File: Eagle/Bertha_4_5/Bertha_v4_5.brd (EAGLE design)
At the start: 100 x 84.6 mm, 136 parts, among them CON1 JACK_DC_BARREL, CON2 JACK_DC_BARREL, IC1 MCP1703DB, IC4 DRV8811, J1 RJ12RIGHTANGLE-I2C, J2 RJ12RIGHTANGLE-I2C, Q5 BSP75, Q6 BSP75, U1 HX711, U100 RN2483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

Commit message: All connectors on the connector slot
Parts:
- removed JP1: (no value), freetronics-master-v1:SCREWTERMINAL-3.5MM-4
- added JP3: (no value), jumper:JP4
- moved X1 37.1 mm to (7.61, -2.08), turned to 180 degrees
- moved CON2 33.7 mm to (19.7, -5.27), turned to 0 degrees
- moved LDM1 26.7 mm to (75.8, 28.6)
- moved R11 26.2 mm to (27.6, 27.7), turned to 270 degrees
- moved RT1 25.7 mm to (8.58, 4.91), turned to 180 degrees
- moved RK11 25.2 mm to (73.2, 30.7)
- moved LDM4 20.5 mm to (78.1, 23.9)
- moved CU8 18.0 mm to (0.41, 19.3), turned to 270 degrees
- moved LDPID 17.1 mm to (24.8, 32.3), turned to 0 degrees
- moved RK8 15.0 mm to (74.0, 25.3)
- moved LDPW12 14.7 mm to (22.3, 32.3), turned to 0 degrees
- moved HX1 13.8 mm to (8.35, 21.2), turned to 180 degrees
- moved RK14 13.5 mm to (24.9, 27.7), turned to 270 degrees
- moved LDPW3 12.9 mm to (19.8, 32.2), turned to 0 degrees
- moved CU7 12.0 mm to (7.25, 12.9), turned to 180 degrees
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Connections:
- net N$10: now also JP3.2; no longer JP1.3
- net N$4: now also JP3.4; no longer JP1.1
- net N$55: now also JP3.1; no longer JP1.4
- net N$56: now also JP3.3; no longer JP1.2
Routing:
- net VDD: track 183.1 -> 119.0 mm, vias 2 -> 1
- net +12V: track 205.8 -> 158.6 mm
- net D6*: track 61.4 -> 26.9 mm
- net N$21: track 22.0 -> 51.6 mm
- net A1: track 48.1 -> 23.5 mm, vias 2 -> 0
- net N$6: track 21.9 -> 2.69 mm
- net N$9: track 35.1 -> 19.1 mm
- net 3.3V: track 430.3 -> 437.7 mm
- net VUSB: track 116.9 -> 113.2 mm
- net N$31: track 1.82 -> 0.00 mm
- net N$37: track 1.80 -> 0.00 mm
- net N$2: track 15.6 -> 17.4 mm
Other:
- board text added: "12V"

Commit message: All connectors BUT the PID on external slot, DRV8811 to be routed closes #57 ref #47
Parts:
- moved CON2 43.3 mm to (-4.99, 30.3), turned to 270 degrees
- moved R11 14.9 mm to (19.2, 15.3), turned to 180 degrees
- moved LDPID 14.3 mm to (23.9, 18.0), turned to 270 degrees
- moved RT1 13.2 mm to (21.7, 3.35)
- moved X1 13.1 mm to (20.7, -2.00)
- moved LDPW12 11.8 mm to (23.8, 20.5), turned to 270 degrees
- moved RK14 11.3 mm to (19.3, 17.9), turned to 180 degrees
- moved C2 10.6 mm to (39.6, 19.2), turned to 90 degrees
- moved LDPW3 9.98 mm to (23.8, 23.0), turned to 270 degrees
- moved HX1 9.87 mm to (7.40, 11.4), turned to 0 degrees
- moved CU4 9.32 mm to (37.3, 19.2), turned to 90 degrees
- moved U$2 8.31 mm to (20.6, 32.6)
- moved 3V3 8.31 mm to (24.8, 29.1)
- moved RT2 8.31 mm to (23.9, 32.6)
- moved R12 7.75 mm to (19.3, 20.6), turned to 180 degrees
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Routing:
- net 3.3V: track 437.7 -> 486.7 mm, vias 14 -> 16
- net +12V: track 158.6 -> 205.6 mm
- net VDD: track 119.0 -> 159.1 mm, vias 1 -> 2
- net N$21: track 51.6 -> 79.3 mm
- net N$6: track 2.69 -> 26.4 mm
- net D6*: track 26.9 -> 50.0 mm
- net N$9: track 19.1 -> 28.6 mm
- net N$2: track 17.4 -> 19.4 mm
- net GND: track 160.9 -> 162.4 mm

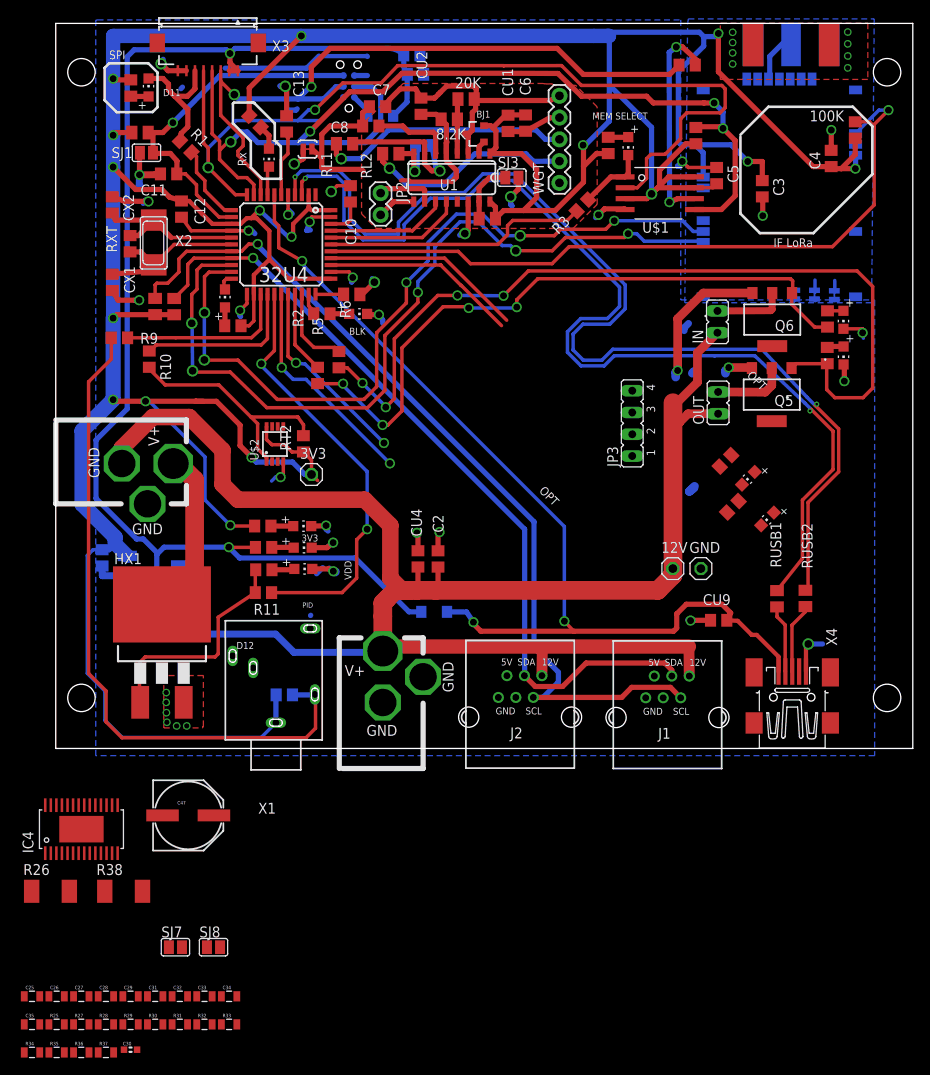
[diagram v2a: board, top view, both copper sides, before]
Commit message: Bertha V4.5 with DRV8811, still need to put the connectors closer to the edge ref #47
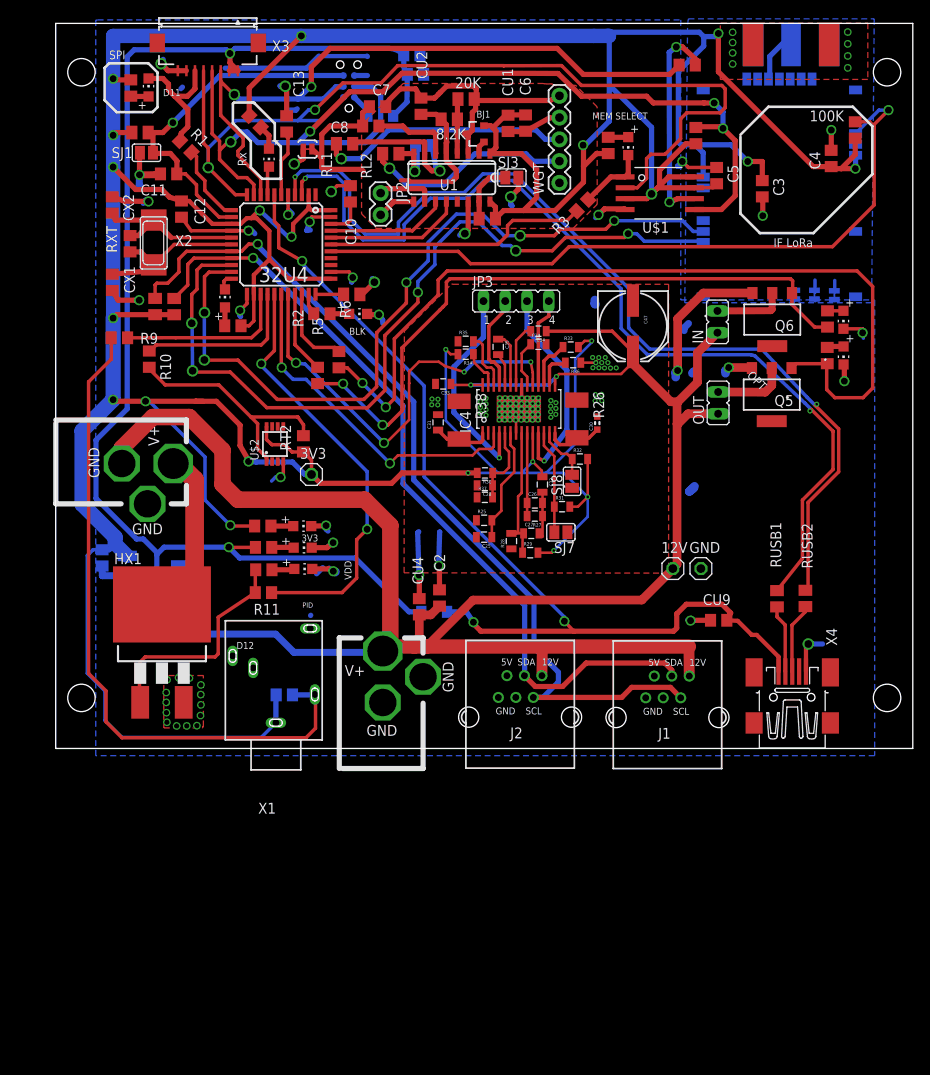
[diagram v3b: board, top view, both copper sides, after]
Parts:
- removed LDM1, LDM4: RED, adafruit:CHIP-LED0805
- removed RK11, RK8: 10K, rcl:R0805
- moved R36 98.8 mm to (55.4, 42.1), turned to 180 degrees
- moved C35 96.0 mm to (46.6, 44.0), turned to 270 degrees
- moved R34 95.9 mm to (42.8, 43.1), turned to 180 degrees
- moved R35 95.7 mm to (42.8, 44.6)
- moved C30 91.2 mm to (58.2, 35.1), turned to 90 degrees
- moved C29 89.7 mm to (51.3, 44.3)
- moved R33 88.5 mm to (55.1, 43.9)
- moved C34 85.6 mm to (51.3, 45.8), turned to 180 degrees
- moved R26 82.5 mm to (55.8, 35.5), turned to 270 degrees
- moved C26 80.2 mm to (50.9, 25.7)
- moved R27 79.5 mm to (50.9, 24.2), turned to 180 degrees
- moved R32 79.2 mm to (56.2, 30.9)
- moved R37 78.4 mm to (45.1, 26.4)
- moved C47 77.1 mm to (62.4, 46.4), turned to 270 degrees
- moved R25 77.1 mm to (45.0, 23.7)
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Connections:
- removed net D3: IC4.3
- removed net D6: IC4.19
- removed net N$31: LDM4.C, RK8.2
- removed net N$37: LDM1.C, RK11.2
- net +12V: no longer LDM1.A, LDM4.A
- net D8*: now also IC4.3
- net D9*: now also IC4.19
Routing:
- net 3.3V: track 486.7 -> 583.7 mm, vias 16 -> 22
- net +12V: track 205.6 -> 244.7 mm, vias 0 -> 2
- net D9*: track 22.5 -> 50.4 mm, vias 2 -> 4
- net N$56: track 0.00 -> 25.1 mm, vias 0 -> 1
- net N$55: track 0.00 -> 24.8 mm, vias 0 -> 1
- net A1: track 23.5 -> 0.00 mm
- net A0: track 22.8 -> 0.00 mm
- net GND: track 162.4 -> 184.3 mm, vias 36 -> 117
- net N$49: track 0.00 -> 15.7 mm
- net D8*: track 25.9 -> 40.4 mm
- net N$45: track 0.00 -> 13.4 mm
- net USB_P: track 124.4 -> 111.2 mm
- net USB_N: track 122.7 -> 109.6 mm
- net N$51: track 0.00 -> 12.1 mm
- net N$10: track 0.00 -> 11.3 mm
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
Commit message: shortened boards by 1mm, closes #68
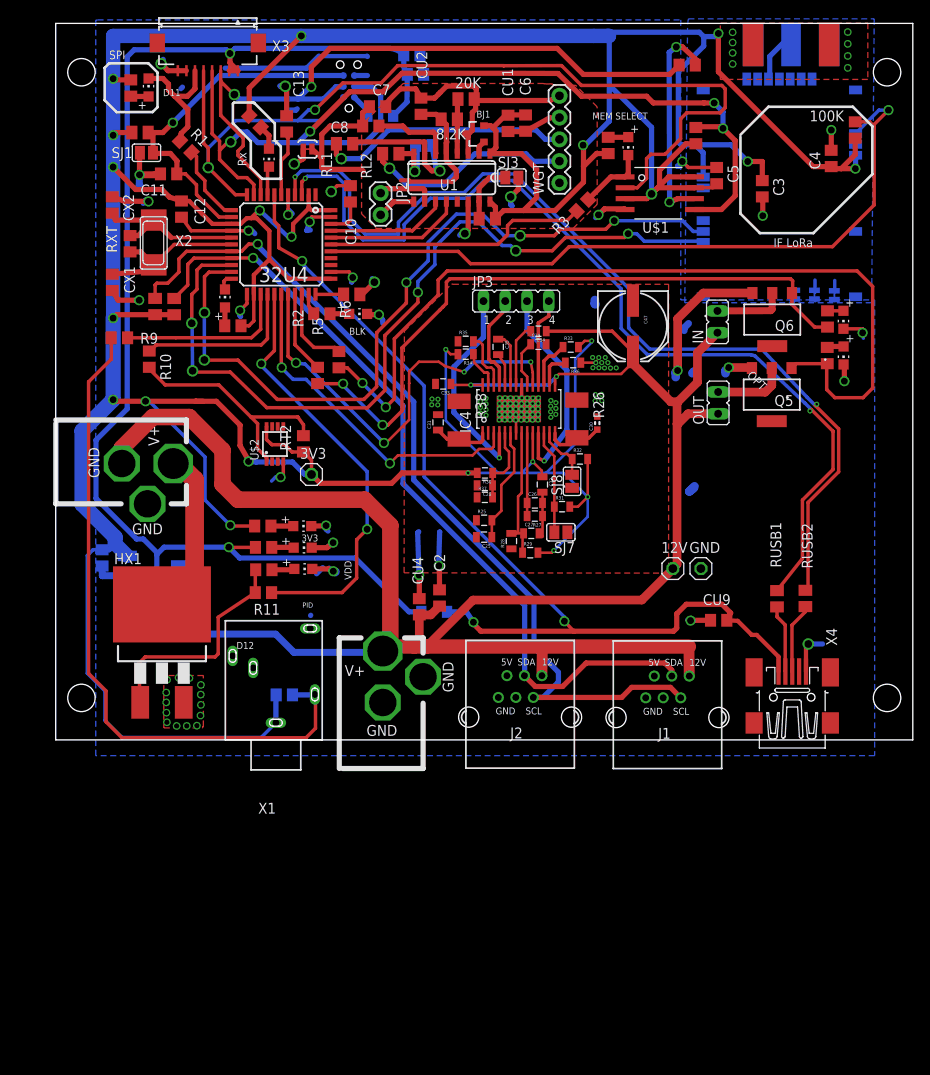
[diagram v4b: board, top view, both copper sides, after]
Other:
- board size 100 x 84.6 mm -> 100 x 83.6 mm

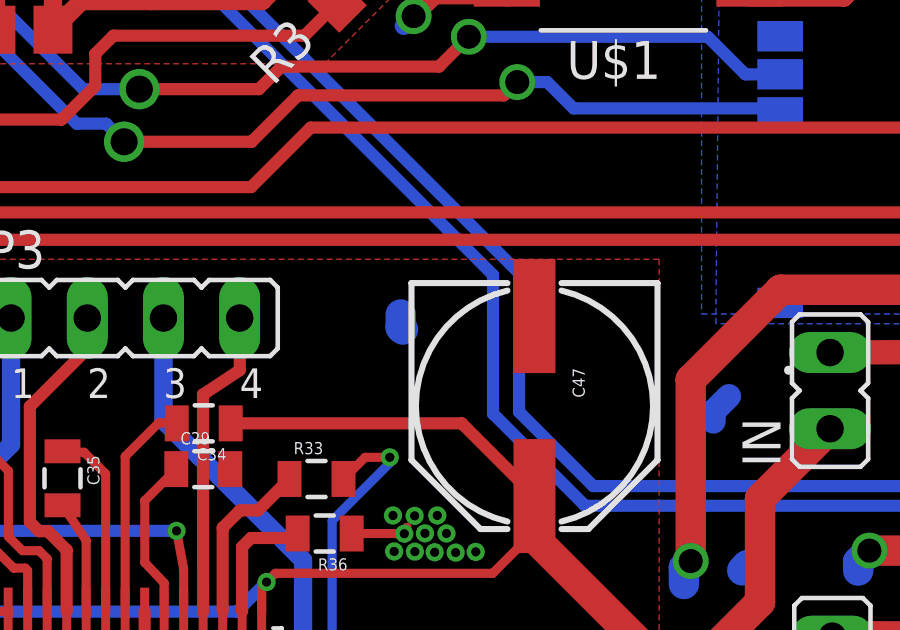
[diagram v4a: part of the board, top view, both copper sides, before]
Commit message: silk screen correction, need to optimize the current limiting resistors on 4.5
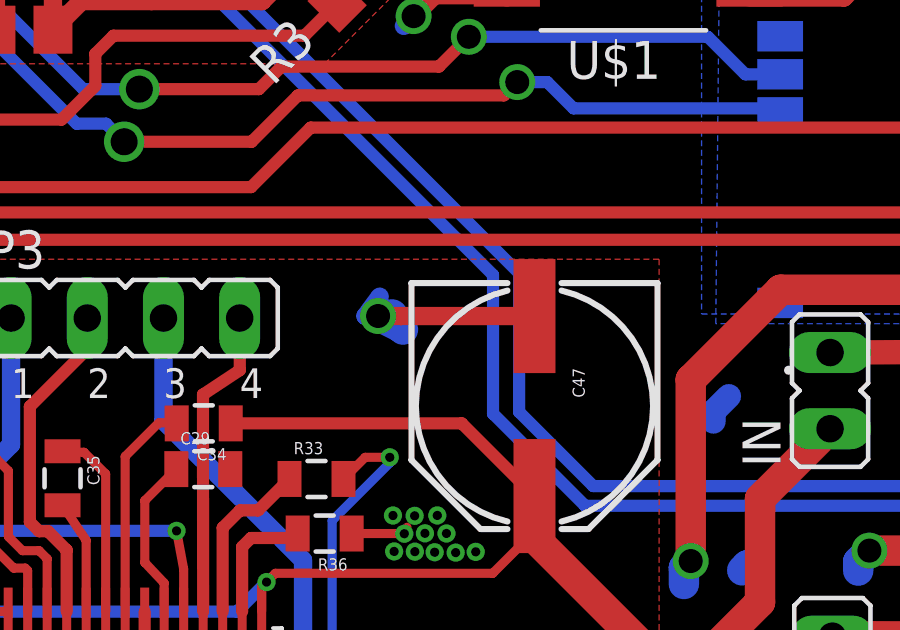
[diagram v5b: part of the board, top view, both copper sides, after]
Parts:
- C27: value 100nF -> 100n
- C29, C34, C35: value 220nF -> 220n
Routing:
- net GND: track 184.3 -> 191.6 mm, vias 117 -> 118

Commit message: changed PID FET part, ref #72
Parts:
- HX1: value IRF3704S -> IPB081N06L3GATMA1
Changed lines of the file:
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@@
 <?xml version="1.0" encoding="utf-8"?>
 <!DOCTYPE eagle SYSTEM "eagle.dtd">
-<eagle version="6.5.0">
+<eagle version="7.5.0">
 <drawing>
 <settings>
@@
 <pass name="Default">
 <param name="RoutingGrid" value="6mil"/>
+<param name="AutoGrid" value="1"/>
+<param name="Efforts" value="0"/>
+<param name="TopRouterVariant" value="1"/>
 <param name="tpViaShape" value="round"/>
 <param name="PrefDir.1" value="|"/>
@@
 </element>
 <element name="RK1" library="resistor" package="M0805" value="10K" x="8.82023125" y="48.6536625" smashed="yes" rot="R90"/>
-<element name="HX1" library="transistor-power" package="D2PACK" value="IRF3704S" x="7.39551875" y="11.3685"/>
+<element name="HX1" library="transistor-power" package="D2PACK" value="IPB081N06L3GATMA1" x="7.39551875" y="11.3685"/>
 <element name="R11" library="rcl" package="R0805" value="1K" x="19.235359375" y="15.283575" smashed="yes" rot="R180">
 <attribute name="NAME" x="21.168603125" y="13.974734375" size="1.27" layer="25" rot="R180"/>

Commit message: correction on PID labelling, closes #71
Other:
- board text added: "+"
- board text added: "-"
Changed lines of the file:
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@@
 <rectangle x1="28.973146875" y1="42.727246875" x2="34.596709375" y2="42.731053125" layer="201"/>
 <rectangle x1="8.7261125" y1="75.08869375" x2="16.8590625" y2="78.89869375" layer="43"/>
-<text x="-0.4163" y="34.536078125" size="1.4224" layer="27" ratio="16" rot="R180">PID</text>
+<text x="-1.071959375" y="38.351040625" size="1.4224" layer="27" ratio="16" rot="R180">PID</text>
 <text x="16.44800625" y="80.96603125" size="1.27" layer="27" ratio="16" rot="R180">Screen</text>
 <text x="88.803746875" y="53.548509375" size="1.778" layer="26" rot="MR0">LoRa RN2483</text>
@@
 <text x="24.90859375" y="25.079815625" size="0.8128" layer="27" ratio="16" rot="R180">3V3</text>
 <text x="30.78368125" y="18.199328125" size="0.8128" layer="27" ratio="16" rot="R180">PID</text>
+<rectangle x1="3.6359" y1="21.876415625" x2="7.4506125" y2="23.42624375" layer="21"/>
+<rectangle x1="-1.3709125" y1="28.5526" x2="0.178815625" y2="32.30795" layer="21"/>
+<rectangle x1="5.126021875" y1="32.24834375" x2="7.331403125" y2="34.573084375" layer="21"/>
+<text x="-0.119209375" y="26.704728125" size="1.778" layer="21">+</text>
+<text x="8.10626875" y="33.02325625" size="1.778" layer="21">-</text>
 </plain>
 <attributes>
